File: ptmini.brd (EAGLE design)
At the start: 60.3 x 64.4 mm, 47 parts, among them J4 MINI-USB-UX60A-MB-5ST, Q1 MMBT2222A, U1 MCP1703DB, U2 CY8C4248AZI-L485, U3 UBLOX_MAX, U4 MS5611-01BA03, U5 EEPROM-I2CSMD, U6 DRA818V, U7 PUSBM12VX4-TL-115

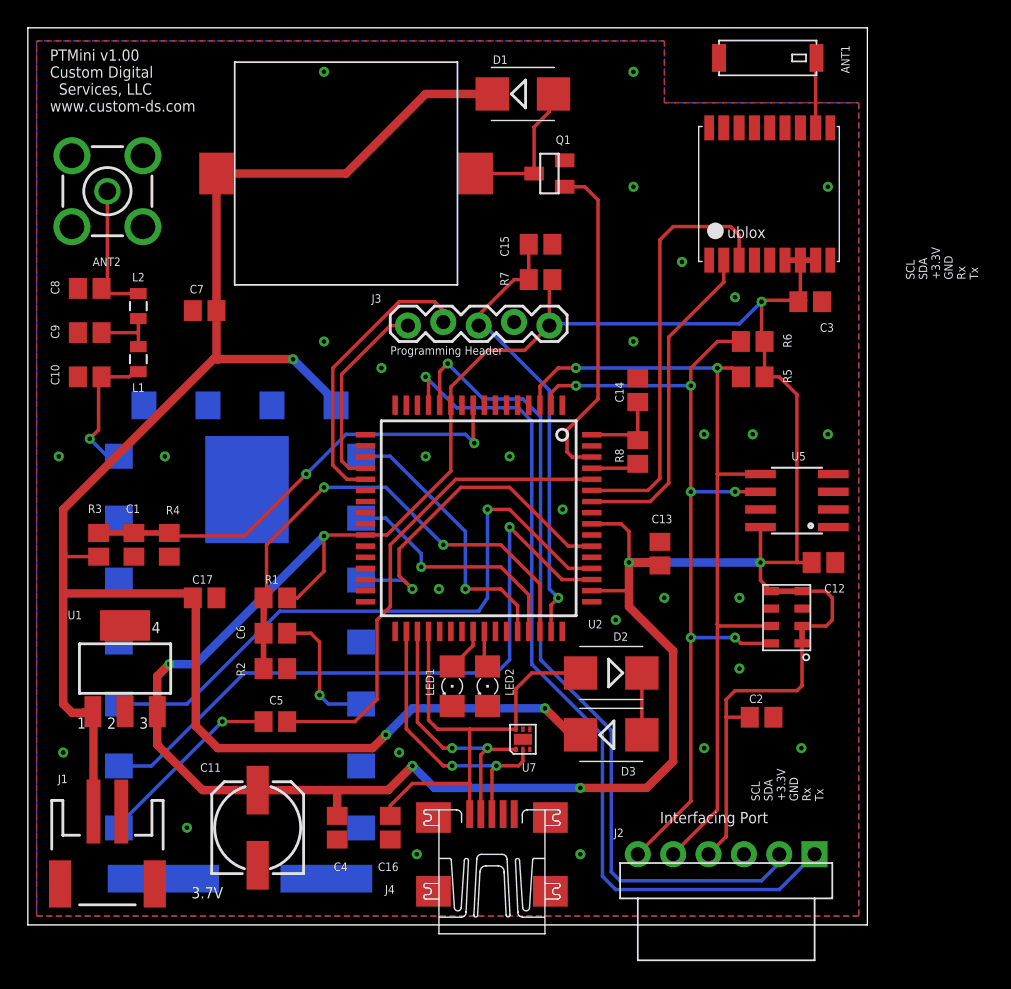
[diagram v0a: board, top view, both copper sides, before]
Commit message: Board version 1.01.
Minor changes to a few of the component libraries.  Swapped out the
diodes with a smaller LL4148 diode.  Defined all component values and
Digikey part numbers.  Set values for low pass filter.  Renumbered board
to 1.01 to reflect the slight layout changes.  All components remain
unchanged otherwise.
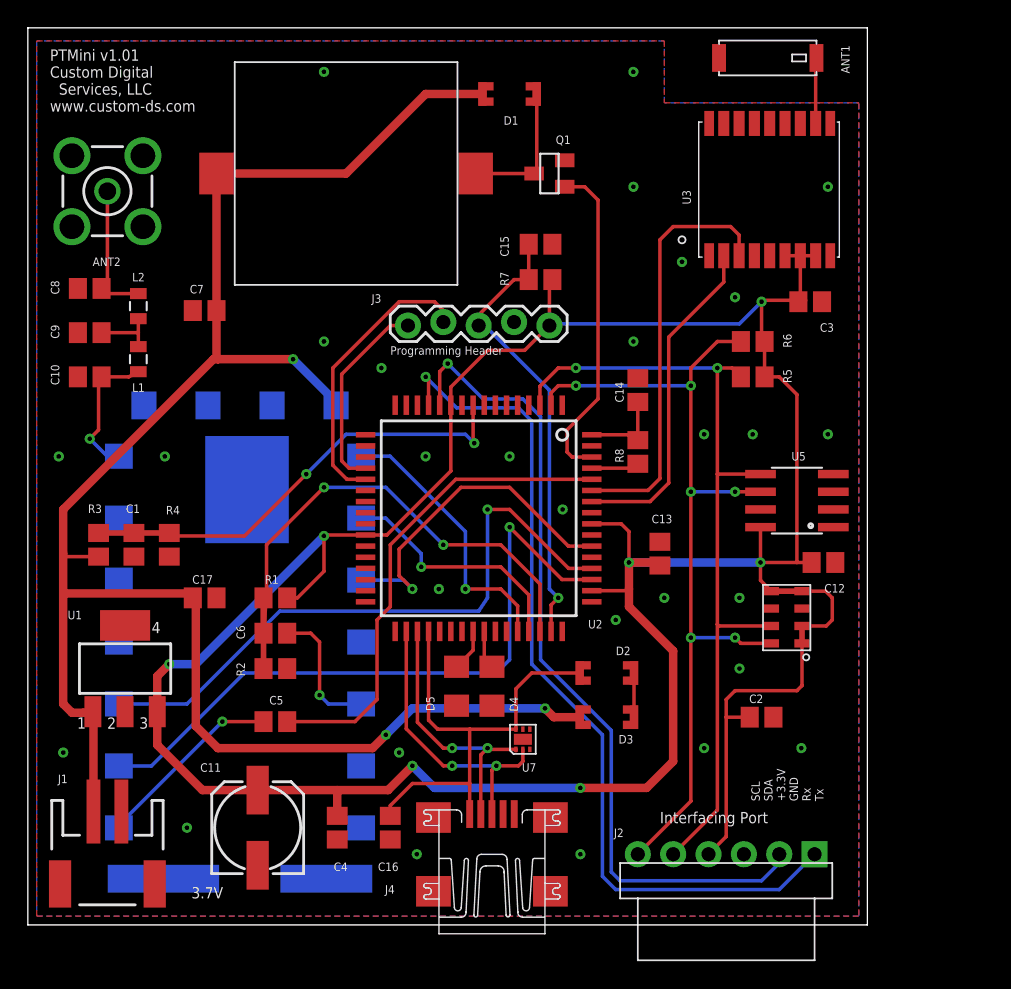
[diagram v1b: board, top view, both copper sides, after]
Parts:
- removed LED1, LED2: (no value), eagle-ltspice:LED_1206
- added D4, D5: LED, custom-ds:DIODE-1206
- C10, C8: value (none) -> 20pF
- C9: value (none) -> 36pF
- D1, D2, D3: value S1BB -> LL4148; device diode:SMB -> custom-ds:SOD-80
- L1, L2: value (none) -> 68nH
- U3: value UBLOX_MAX -> UBLOX-MAX; device Ava:UBLOX_MAX -> custom-ds:UBLOX-MAX
- moved D3 1.31 mm to (41.6, 14.9), turned to 180 degrees
- moved D1 0.95 mm to (34.6, 59.7), turned to 180 degrees
- moved U3 0.32 mm to (53.3, 53.0), turned to 90 degrees
- moved D2 0.32 mm to (41.6, 18.1), turned to 0 degrees
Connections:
- net 9_V_RESET renamed RESET
- removed net N$3: D2.C, D3.A
- new net N$5: D2.CATHODE, D3.ANODE
- net GND: now also D4.CATHODE, D5.CATHODE; no longer LED1.C, LED2.C
- net LED_STATUS: now also D5.ANODE; no longer LED1.A
- net LED_XMIT: now also D4.ANODE; no longer LED2.A
- net N$1: now also D1.ANODE; no longer D1.A
- net USB_VBUS: now also D2.ANODE; no longer D2.A
- net V+: now also D1.CATHODE, D3.CATHODE; no longer D1.C, D3.C
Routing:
- net N$3: track 4.45 -> 0.00 mm
- net N$5: track 0.00 -> 3.18 mm
- net V+: track 136.3 -> 135.0 mm
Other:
- board text added: "PTMini v1.01 Custom Digital Services, LLC www.custom-ds.com"
- board text removed: "PTMini v1.00 Custom Digital Services, LLC www.custom-ds.com"

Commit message: Board version 1.1.0
Fixed incorrect chip footprint for PSoC chip, and also a bad power
connection to the chip.  Relocated the piezo to the back side of the PCB
and consolidated down to 5cm x 6cm.
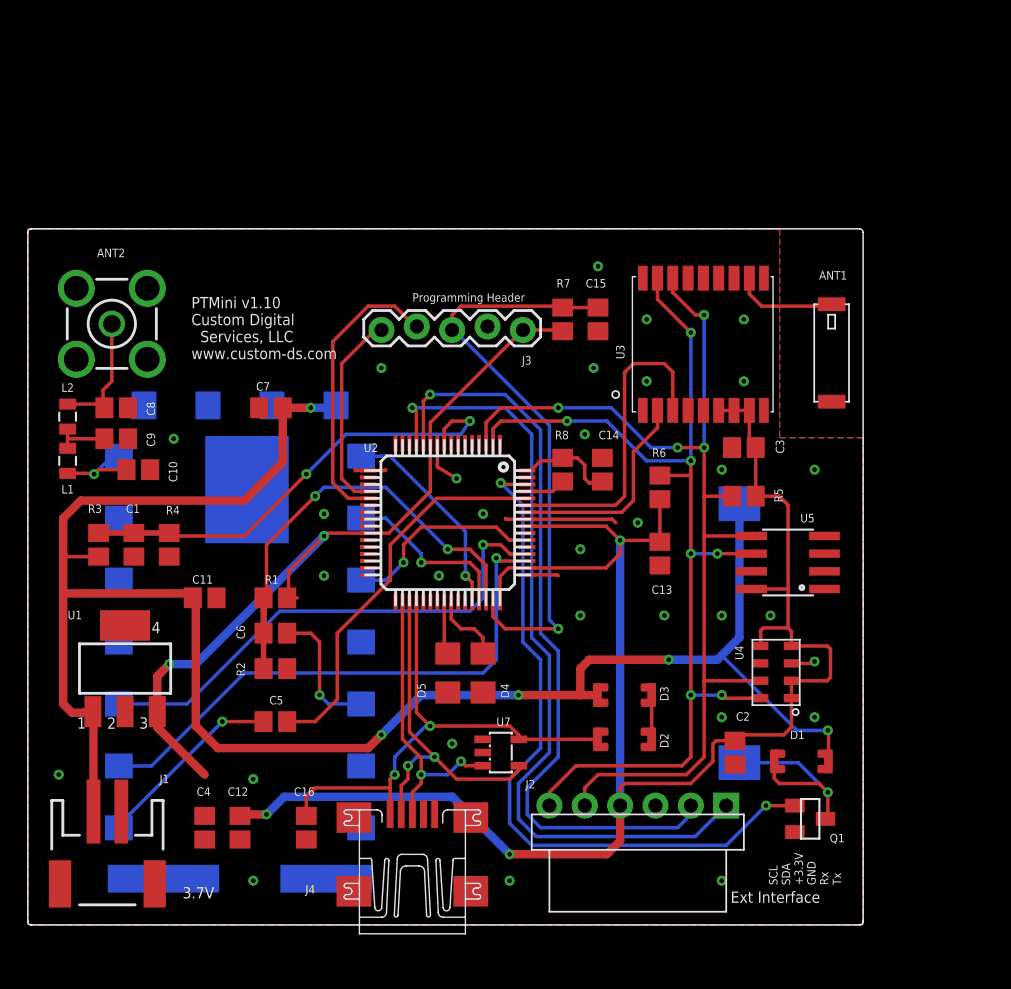
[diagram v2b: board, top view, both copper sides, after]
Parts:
- removed C17: .1uF, resistor:C0805
- C11: value 47uF -> .1uF; device resistor:153CLV-0605 -> resistor:C0805
- C4: value .1uF -> 10uF
- U2: device custom-ds:QFP64_SOT393 -> custom-ds:TQFP64-10X10
- U3: value UBLOX-MAX -> UBLOX MAX-M8Q
- U4: value MS5611-01BA03 -> TE-BARO-SENSOR-MS5611-01BA03; device TE Connectivity Baro Sensor:MS5611-01BA03 -> custom-ds:TE-BARO-SENSOR-MS5611-01BA3
- U7: value PUSBM12VX4-TL-115 -> WURTH-824011-TVS-ARRAY; device custom-ds:PUSBM12VX4-TL-115 -> custom-ds:SOT23-5
- moved D1 52.3 mm to (55.6, 11.7), turned to 0 degrees
- moved Q1 50.0 mm to (56.2, 7.62), turned to 270 degrees
- moved C12 46.0 mm to (15.2, 6.99), turned to 270 degrees
- moved SG1 43.5 mm to (51.1, 21.0), flipped to the bottom, turned to 270 degrees
- moved C11 16.9 mm to (12.7, 23.5), turned to 0 degrees
- moved ANT1 16.3 mm to (58.7, 45.1), turned to 270 degrees
- moved R6 12.4 mm to (45.4, 31.4), turned to 270 degrees
- moved U3 12.1 mm to (48.6, 41.9)
- moved C3 11.5 mm to (51.4, 34.3), turned to 180 degrees
- moved ANT2 9.53 mm to (6.03, 43.2)
- moved C4 9.53 mm to (12.7, 6.99)
- moved L2 9.42 mm to (2.86, 36.5)
- moved L1 8.90 mm to (2.86, 33.3)
- moved C8 8.78 mm to (6.35, 37.1), turned to 0 degrees
- moved R5 8.60 mm to (51.4, 30.8)
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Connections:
- net +3V3: now also U2.48, U4.1, U4.2, U4.4, U4.5; no longer C11.+, U4.P$1, U4.P$2, U4.P$4, U4.P$5
- net GND: now also C11.2, U4.3, U7.2; no longer C11.-, C17.2, U2.48, U4.P$3, U7.P$7
- net SCL: now also U3.17_SCL2, U4.8; no longer U4.P$8
- net SDA: now also U3.16_SDA2, U4.7; no longer U4.P$7
- net USB_D+: now also U7.3; no longer U7.P$2
- net USB_D-: now also U7.4; no longer U7.P$1
- net USB_VBUS: now also U7.5; no longer U7.P$6
- net V+: now also C11.1; no longer C17.1
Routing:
- net +3V3: track 220.2 -> 188.9 mm, vias 7 -> 5
- net PIEZO: track 23.7 -> 50.8 mm, vias 0 -> 2
- net GND: track 0.00 -> 17.6 mm, vias 29 -> 31
- net SDA: track 59.9 -> 74.7 mm, vias 2 -> 4
- net SCL: track 63.1 -> 76.1 mm, vias 6 -> 7
- net PTT: track 24.6 -> 14.6 mm
- net XRES: track 32.8 -> 42.6 mm
- net GPS_RX: track 24.0 -> 15.2 mm
- net VHF_TX: track 45.3 -> 36.6 mm
- net VHF_RX: track 48.2 -> 39.9 mm
- net GPS_TX: track 30.2 -> 22.9 mm
- net TX_AUDIO: track 35.0 -> 28.2 mm
- net USB_D-: track 19.4 -> 25.0 mm
- net RX_AUDIO: track 41.6 -> 36.4 mm
- net AUX232_TX: track 62.6 -> 57.5 mm
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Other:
- board size 60.3 x 64.4 mm -> 60 x 50 mm
- board text added: "Ext Interface"
- board text added: "PTMini v1.10 Custom Digital Services, LLC www.custom-ds.com"
- board text removed: "Interfacing Port"
- board text removed: "PTMini v1.01 Custom Digital Services, LLC www.custom-ds.com"
